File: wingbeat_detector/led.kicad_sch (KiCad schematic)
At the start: 9 parts, among them J2 CONN_UMC_JACK_SMD, Q1 MOSFET-N-CH, U6 LED_DRV_50mA

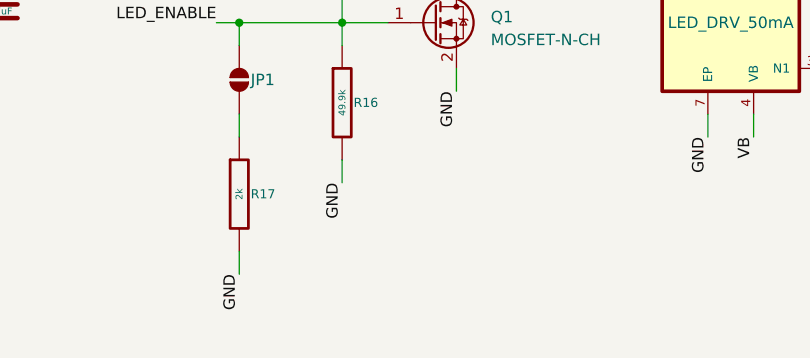
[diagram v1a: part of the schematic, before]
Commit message: Copy edge cuts to documentation layers
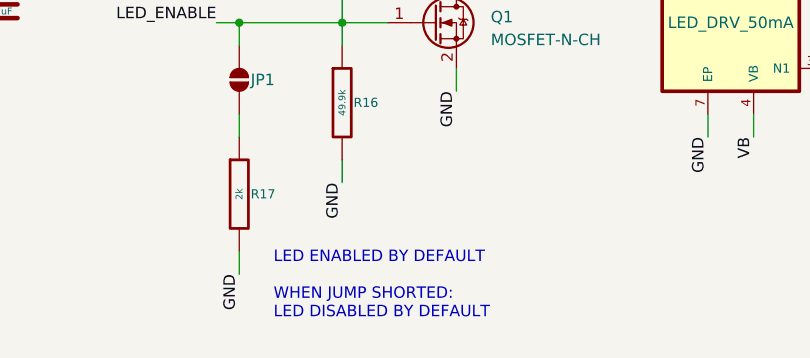
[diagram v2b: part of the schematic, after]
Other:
- note added: "LED ENABLED BY DEFAULT WHEN JUMP SHORTED: LED DISABLED BY DEFAULT"
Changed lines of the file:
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@@
   (title_block
     (title "wingbeat_detector")
-    (date "2023-03-21")
+    (date "2023-03-22")
     (rev "3.0")
     (company "Howard Hughes Medical Institute")
@@
     (effects (font (size 1.27 1.27)) (justify left bottom))
   )
+  (text "LED ENABLED BY DEFAULT\n\nWHEN JUMP SHORTED:\nLED DISABLED BY DEFAULT"
+    (at 148.59 121.92 0)
+    (effects (font (size 1.27 1.27)) (justify left bottom))
+  )

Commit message: Finished layout for v3.0
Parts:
- J2: value CONN_UMC_JACK_SMD -> UMC_JACK_SMD
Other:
- company: Howard Hughes Medical Institute -> Peter Polidoro
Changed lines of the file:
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@@
   (title_block
     (title "wingbeat_detector")
-    (date "2023-03-22")
+    (date "2023-03-23")
     (rev "3.0")
-    (company "Howard Hughes Medical Institute")
+    (company "Peter Polidoro")
   )
   (junction (at 156.21 88.9) (diameter 0) (color 0 0 0 0)
@@
       (effects (font (size 1.27 1.27)) (justify left))
     )
-    (property "Value" "CONN_UMC_JACK_SMD" (at 93.091 111.76 90)
-      (effects (font (size 1.27 1.27)) hide)
-    )
+    (property "Value" "UMC_JACK_SMD" (at 93.091 111.76 90)
+      (effects (font (size 1.27 1.27)) hide)
+    )
